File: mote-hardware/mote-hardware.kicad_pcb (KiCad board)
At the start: 2 copper layers, 93.6 x 102.8 mm, 67 parts, among them J1 USB_C_Receptacle_USB2.0_14P, J2 JST_XH2.54-SP, J4 SM03B-SRSS-TB, J5 Conn_01x03_Pin, J6 Conn_01x03_Pin, J7 JST_PH_B6B, J8 JST_PH_B6B, SW1 SW_Push, SW2 SW_Push, U1 RP2354_60QFN, U2 NCP1117-3.3_SOT223, U4 RP Radio Module 2, U5 DRV8833PW, U9 LSM6DS3, Y1 ABM8-272-T3

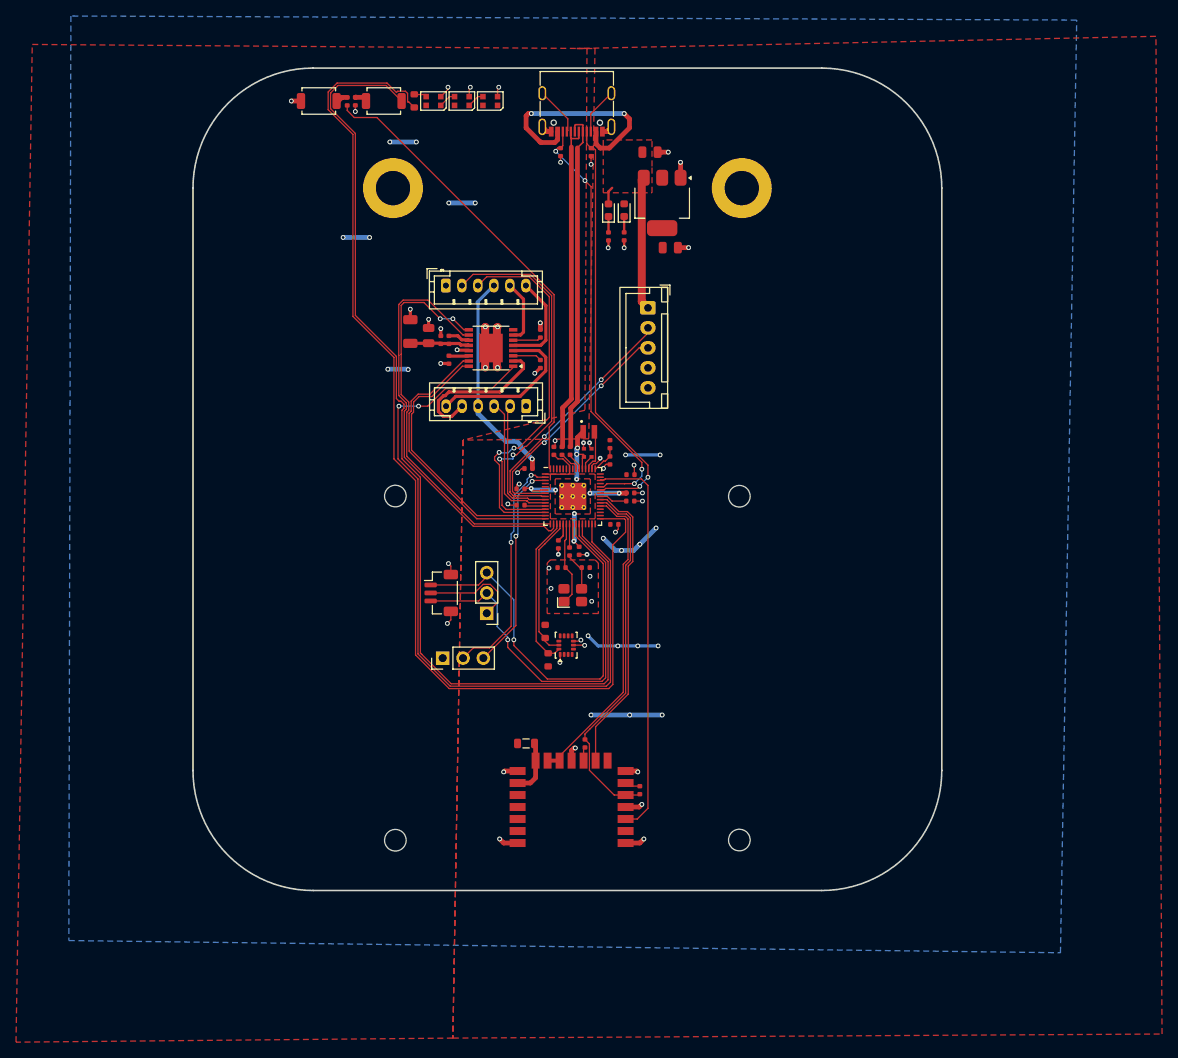
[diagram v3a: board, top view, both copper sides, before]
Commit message: Tear drops, silk screen, screw connectors only on one side
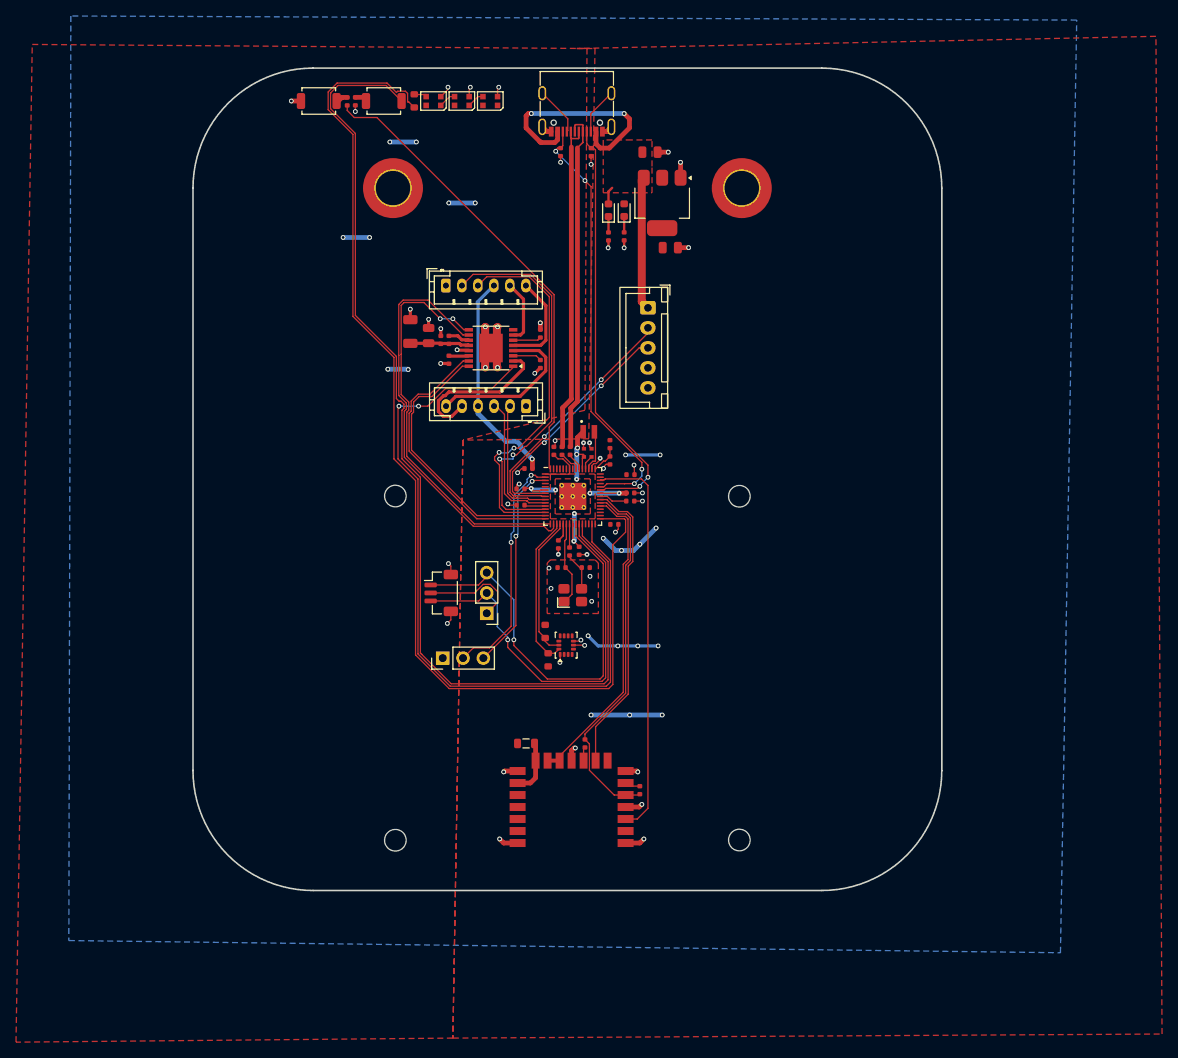
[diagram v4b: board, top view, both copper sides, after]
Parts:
- C22: value 0.1u -> 100n
- H5, H6: footprint MountingHole:MountingHole_4.3mm_M4_DIN965_Pad -> MountingHole:MountingHole_4.3mm_M4_DIN965_Pad_TopOnly
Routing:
- net GND: track 87.7 -> 87.1 mm
- net /lidar_rx: track 32.3 -> 31.7 mm
- net /rp2354/VREG_LX: track 5.52 -> 5.01 mm
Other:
- board text added: "┳┳┓┏┓┏┳┓┏┓ ┃ Robotics for everyone ┃┃┃┃┃ ┃ ┣ ┃ v0.1.0 ┛ ┗┗┛ ┻ ┗┛ ┃ empriselab.github.io/mote-core/"

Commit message: Top side silk screen
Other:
- board text added: "->"
- board text added: "3.3v"
- board text added: "5.0v"
- board text added: "<~~ Motor"
- board text added: "Boot"
- board text added: "Err"
- board text added: "Gnd"
- board text added: "LiDAR"
- board text added: "Pwr"
- board text added: "RX"
- board text added: "Run"
- board text added: "SWD"
- board text added: "SwClk"
- board text added: "Swd"
- board text added: "TX"
- board text added: "UART"
- board text added: "WiFi"
- board text added: "x"
- board text added: "y"
- board text added: "z"
